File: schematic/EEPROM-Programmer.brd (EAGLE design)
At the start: 100 x 80 mm, 8 parts

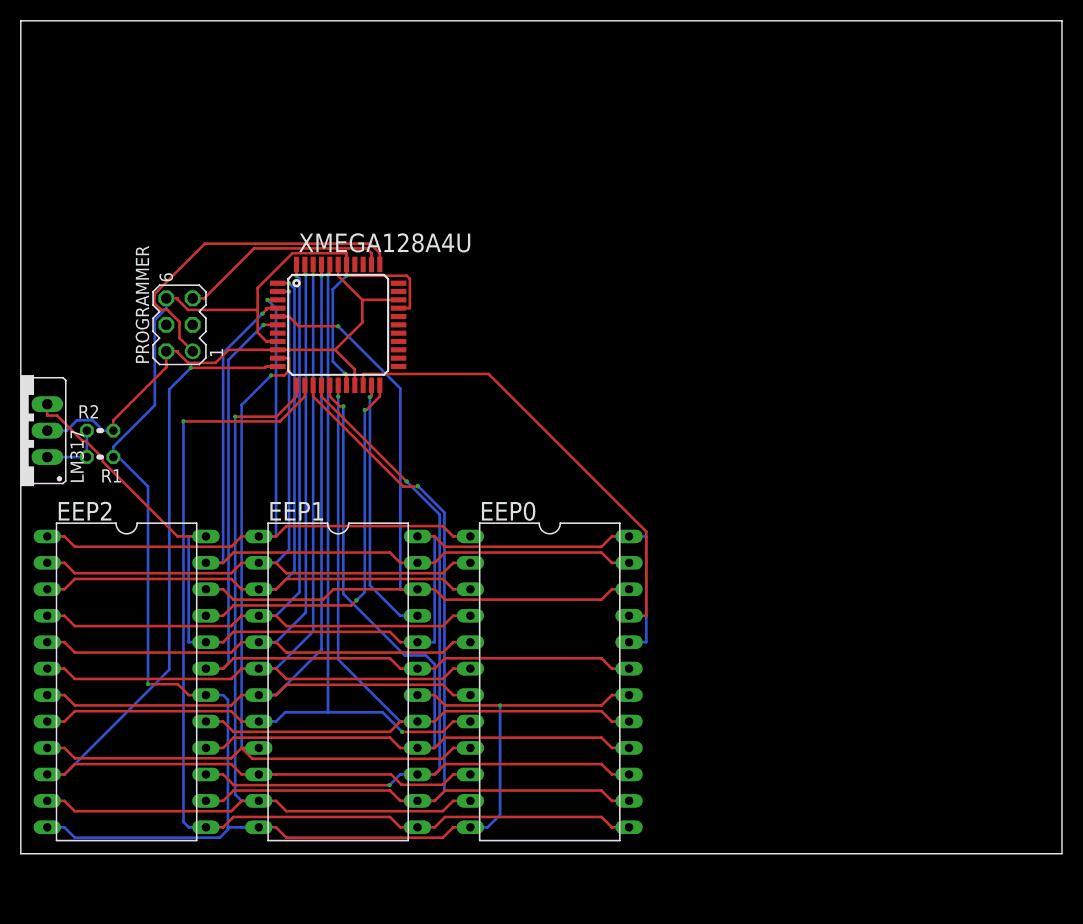
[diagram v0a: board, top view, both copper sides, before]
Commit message: Changed the circuit to only write to one EEPROM
Removed all extra control lines and chips.
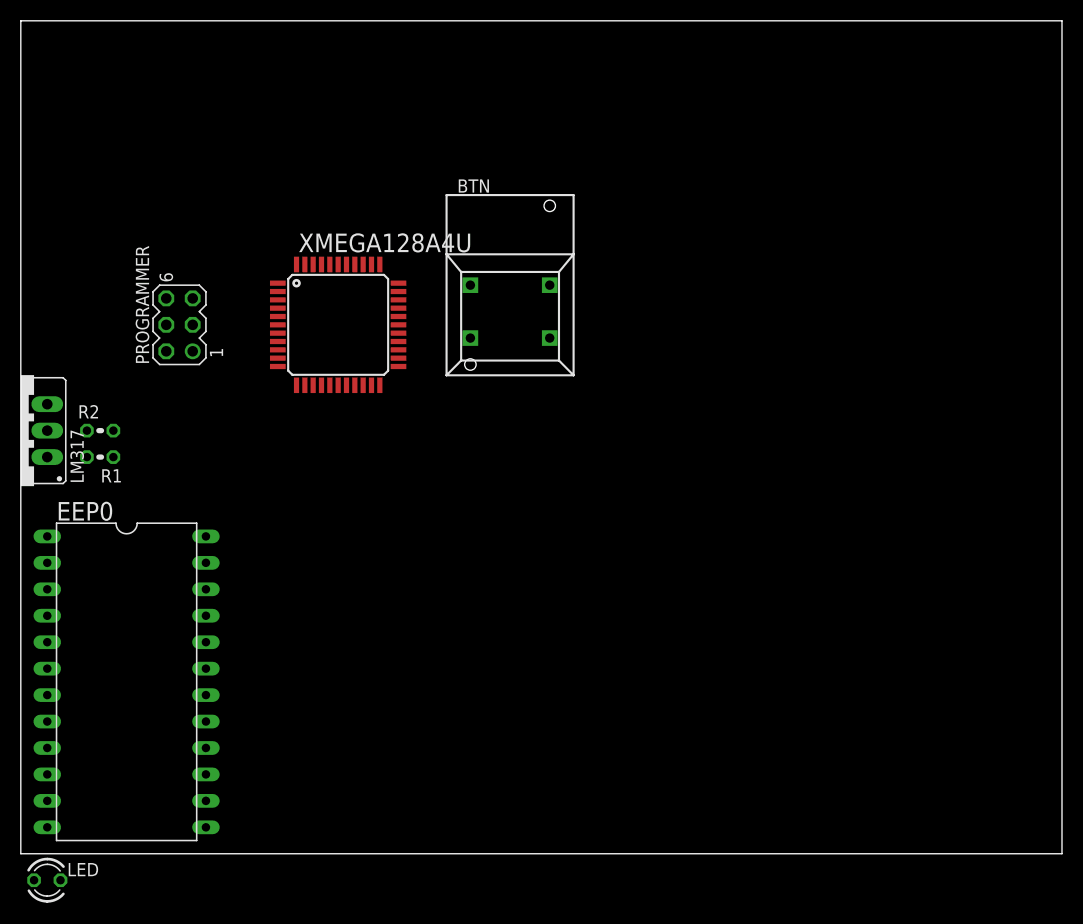
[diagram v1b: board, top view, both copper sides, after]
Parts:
- removed EEP1, EEP2: (no value), memory:DIL24
- added BTN: 5501, switch:5501
- added LED: (no value), led:LED3MM
- moved EEP0 40.6 mm to (10.2, 16.5)
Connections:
- removed net WE1: EEP1.21, XMEGA128A4U.21
- removed net WE2: EEP2.21, XMEGA128A4U.22
- new net BTN: BTN.1A, BTN.1B, XMEGA128A4U.37
- new net LED: LED.K, XMEGA128A4U.36
- net +3V3: now also BTN.NO, LED.A
- net A0: no longer EEP1.8, EEP2.8
- net A1: no longer EEP1.7, EEP2.7
- net A10: no longer EEP1.19, EEP2.19
- net A2: no longer EEP1.6, EEP2.6
- net A3: no longer EEP1.5, EEP2.5
- net A4: no longer EEP1.4, EEP2.4
- net A5: no longer EEP1.3, EEP2.3
- net A6: no longer EEP1.2, EEP2.2
- net A7: no longer EEP1.1, EEP2.1
- net A8: no longer EEP1.23, EEP2.23
- net A9: no longer EEP1.22, EEP2.22
- net D0: no longer EEP1.9, EEP2.9
- net D1: no longer EEP1.10, EEP2.10
- net D2: no longer EEP1.11, EEP2.11
- net D3: no longer EEP1.13, EEP2.13
- net D4: no longer EEP1.14, EEP2.14
- net D5: no longer EEP1.15, EEP2.15
- net D6: no longer EEP1.16, EEP2.16
- net D7: no longer EEP1.17, EEP2.17
- net GND: no longer EEP1.12, EEP1.18, EEP2.12, EEP2.18
- net VCC: no longer EEP1.20, EEP1.24, EEP2.20, EEP2.24
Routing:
- net GND: track 188.8 -> 0.00 mm, vias 4 -> 0
- net VCC: track 104.0 -> 0.00 mm
- net D3: track 96.9 -> 0.00 mm, vias 1 -> 0
- net D1: track 96.4 -> 0.00 mm, vias 1 -> 0
- net D4: track 90.4 -> 0.00 mm, vias 1 -> 0
- net D2: track 88.9 -> 0.00 mm, vias 1 -> 0
- net A1: track 87.1 -> 0.00 mm, vias 1 -> 0
- net D0: track 86.8 -> 0.00 mm, vias 1 -> 0
- net D5: track 86.2 -> 0.00 mm, vias 2 -> 0
- net A0: track 86.1 -> 0.00 mm, vias 2 -> 0
- net D6: track 84.3 -> 0.00 mm, vias 1 -> 0
- net A2: track 84.2 -> 0.00 mm, vias 1 -> 0
- net A3: track 81.4 -> 0.00 mm, vias 1 -> 0
- net A10: track 79.9 -> 0.00 mm, vias 1 -> 0
- net A4: track 78.7 -> 0.00 mm, vias 1 -> 0
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
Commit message: Used Freerouting to route the board
Renamed a few lines.
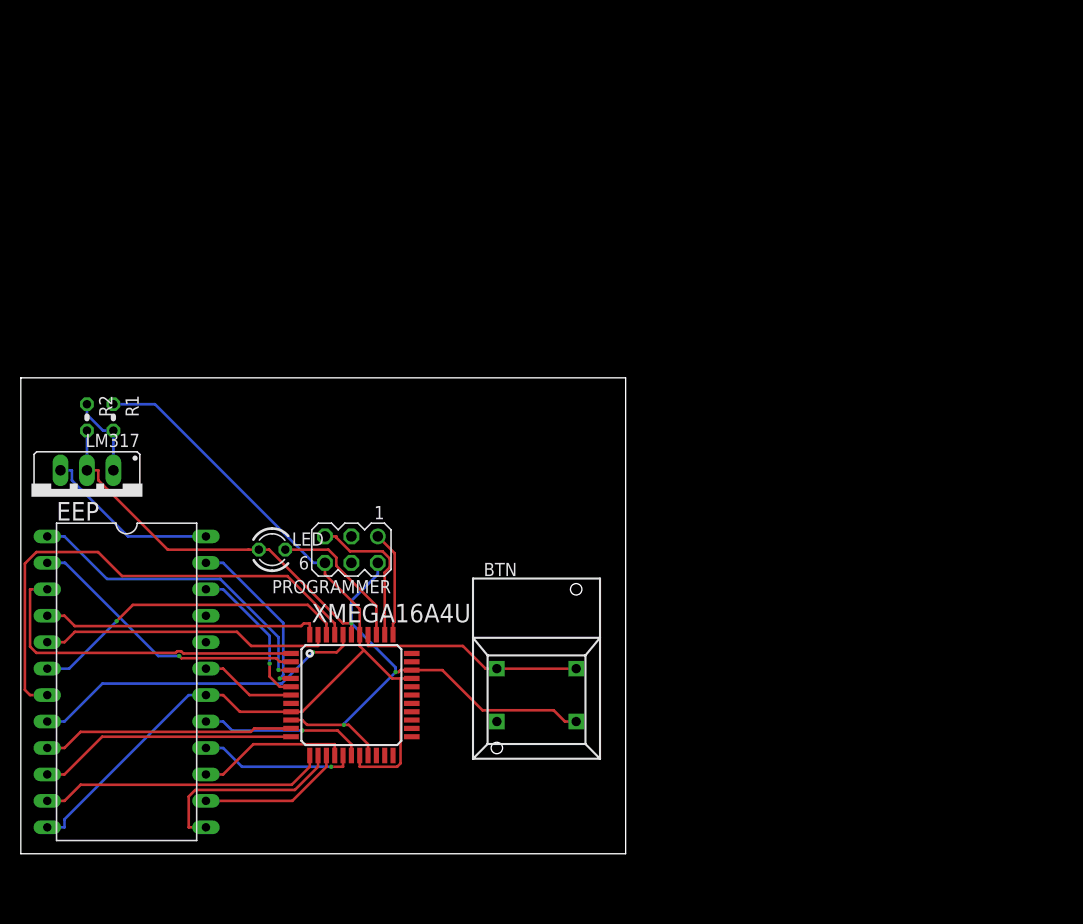
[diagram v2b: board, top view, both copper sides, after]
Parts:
- removed XMEGA128A4U: XMEGA16A4A, atmel:TQFP44
- added XMEGA16A4U: XMEGA16A4A, atmel:TQFP44
- moved LED 38.4 mm to (24.1, 29.2)
- moved BTN 36.9 mm to (49.5, 17.8)
- moved PROGRAMMER 27.2 mm to (31.8, 29.2), turned to 180 degrees
- moved LM317 8.98 mm to (6.35, 34.3), turned to 180 degrees
- moved R1 4.02 mm to (8.89, 41.9), turned to 270 degrees
- moved R2 1.80 mm to (6.35, 41.9), turned to 270 degrees
- renumbered EEP0 to EEP
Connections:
- removed net WE0: EEP.21, XMEGA128A4U.20
- new net OE: EEP.20
- new net WE: EEP.21
- net +3V3: now also XMEGA16A4U.19, XMEGA16A4U.31, XMEGA16A4U.39, XMEGA16A4U.9; no longer XMEGA128A4U.19, XMEGA128A4U.31, XMEGA128A4U.39, XMEGA128A4U.9
- net A0: now also XMEGA16A4U.40; no longer XMEGA128A4U.40
- net A1: now also XMEGA16A4U.41; no longer XMEGA128A4U.41
- net A10: now also XMEGA16A4U.6; no longer XMEGA128A4U.6
- net A2: now also XMEGA16A4U.42; no longer XMEGA128A4U.42
- net A3: now also XMEGA16A4U.43; no longer XMEGA128A4U.43
- net A4: now also XMEGA16A4U.44; no longer XMEGA128A4U.44
- net A5: now also XMEGA16A4U.1; no longer XMEGA128A4U.1
- net A6: now also XMEGA16A4U.2; no longer XMEGA128A4U.2
- net A7: now also XMEGA16A4U.3; no longer XMEGA128A4U.3
- net A8: now also XMEGA16A4U.4; no longer XMEGA128A4U.4
- net A9: now also XMEGA16A4U.5; no longer XMEGA128A4U.5
- net BTN: now also XMEGA16A4U.37; no longer XMEGA128A4U.37
- net D0: now also XMEGA16A4U.10; no longer XMEGA128A4U.10
- net D1: now also XMEGA16A4U.11; no longer XMEGA128A4U.11
- net D2: now also XMEGA16A4U.12; no longer XMEGA128A4U.12
- net D3: now also XMEGA16A4U.13; no longer XMEGA128A4U.13
- net D4: now also XMEGA16A4U.14; no longer XMEGA128A4U.14
- net D5: now also XMEGA16A4U.15; no longer XMEGA128A4U.15
- net D6: now also XMEGA16A4U.16; no longer XMEGA128A4U.16
- net D7: now also XMEGA16A4U.17; no longer XMEGA128A4U.17
- net GND: now also XMEGA16A4U.18, XMEGA16A4U.30, XMEGA16A4U.38, XMEGA16A4U.8; no longer XMEGA128A4U.18, XMEGA128A4U.30, XMEGA128A4U.38, XMEGA128A4U.8
- net LED: now also XMEGA16A4U.36; no longer XMEGA128A4U.36
- net PDI_CLK: now also XMEGA16A4U.35; no longer XMEGA128A4U.35
- net PDI_DATA: now also XMEGA16A4U.34; no longer XMEGA128A4U.34
- net VCC: no longer EEP.20
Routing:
- net GND: track 0.00 -> 94.8 mm
- net +3V3: track 0.00 -> 86.3 mm, vias 0 -> 3
- net A1: track 0.00 -> 48.6 mm
- net A5: track 0.00 -> 32.6 mm
- net A0: track 0.00 -> 32.5 mm, vias 0 -> 1
- net A2: track 0.00 -> 31.2 mm, vias 0 -> 1
- net A7: track 0.00 -> 30.6 mm, vias 0 -> 1
- net A3: track 0.00 -> 28.1 mm
- net D2: track 0.00 -> 27.6 mm
- net A6: track 0.00 -> 27.3 mm, vias 0 -> 1
- net A4: track 0.00 -> 26.8 mm
- net D1: track 0.00 -> 24.9 mm
- net D0: track 0.00 -> 24.2 mm
- net BTN: track 0.00 -> 22.0 mm
- net D3: track 0.00 -> 19.3 mm
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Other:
- board size 100 x 80 mm -> 58.1 x 45.7 mm
